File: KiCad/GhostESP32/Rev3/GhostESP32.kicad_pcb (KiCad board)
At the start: 2 copper layers, 60 x 37 mm, 46 parts, among them J1 CONN_02X05, J2 USB_OTG, J3 CONN_01X14, J4 CONN_01X10, Q1 Q_NPN_BEC, Q2 Q_NPN_BEC, Q3 Q_NPN_BEC, SW1 SW_SPDT, U1 MPU-9250, U2 NCP1117ST33T3G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

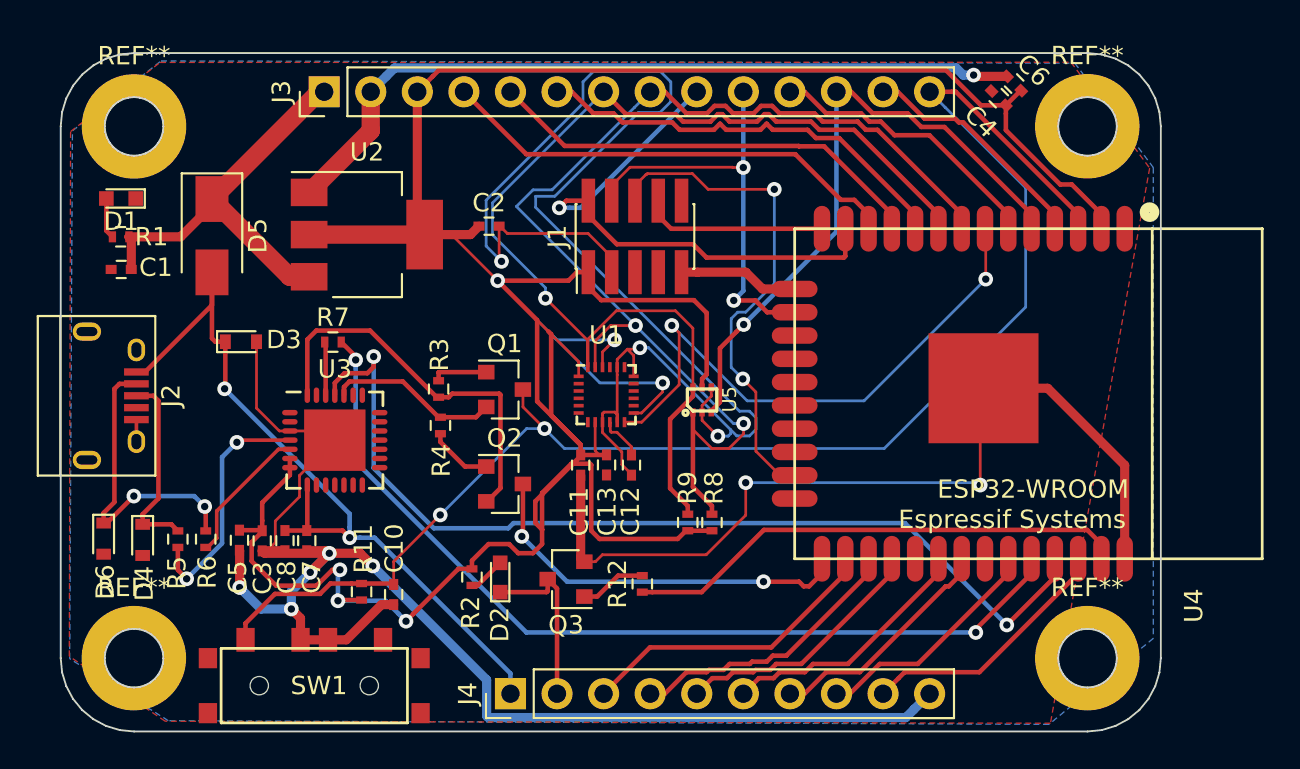
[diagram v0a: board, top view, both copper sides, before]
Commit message: Started on Rev 4 of the ESP32 PCB
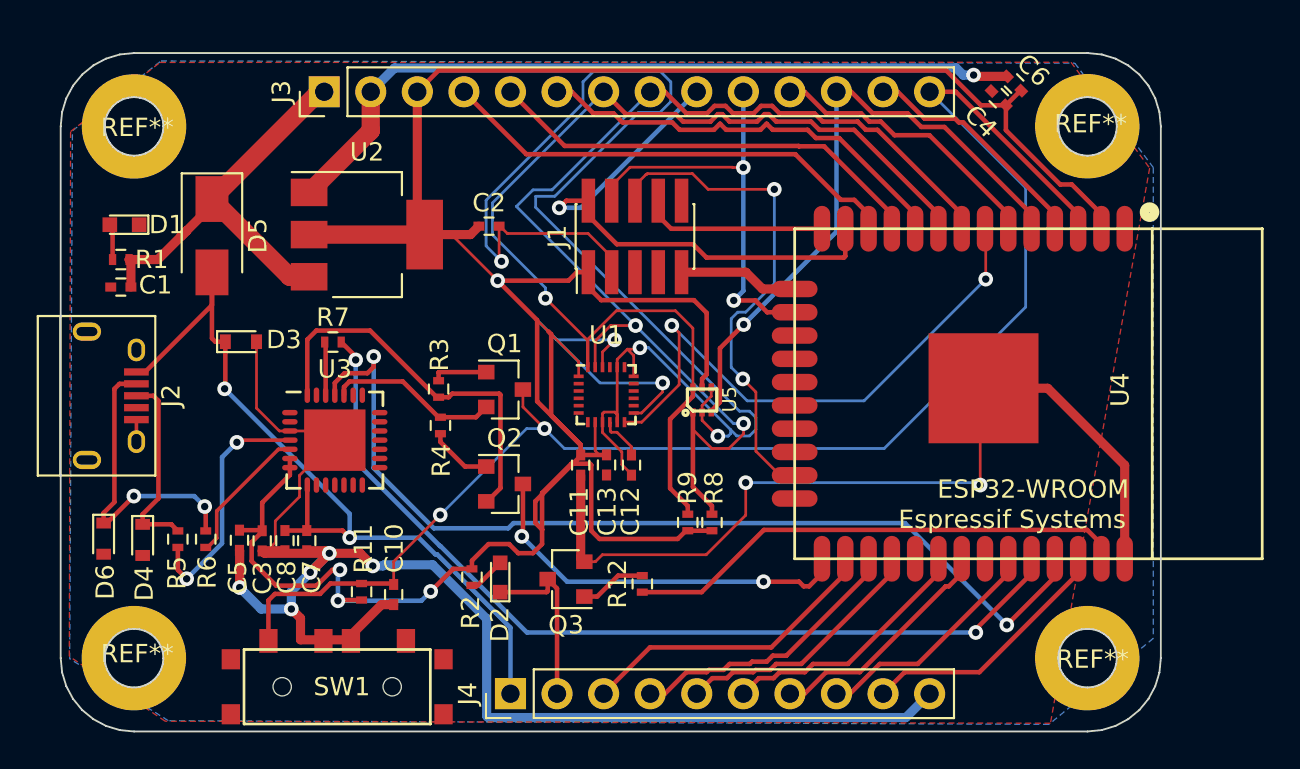
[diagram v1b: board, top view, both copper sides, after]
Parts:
- moved D1 1.44 mm to (116.6, 88.4)
- moved SW1 1.25 mm to (128.2, 113.6)
- moved R1 1.24 mm to (116.4, 90.3)
- moved C1 0.96 mm to (116.4, 91.8)
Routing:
- net GND: track 256.7 -> 258.7 mm
- net VBUS: track 44.5 -> 45.9 mm
- net +3V3: track 184.1 -> 183.2 mm
- net +BATT: track 23.0 -> 23.7 mm
